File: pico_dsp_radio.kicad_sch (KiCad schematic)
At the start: 12 parts, among them J1 Conn_01x02, Q1 IRLML6402, SW1 SW_SPDT, U1 Pico, U2 MCP73831-2-OT

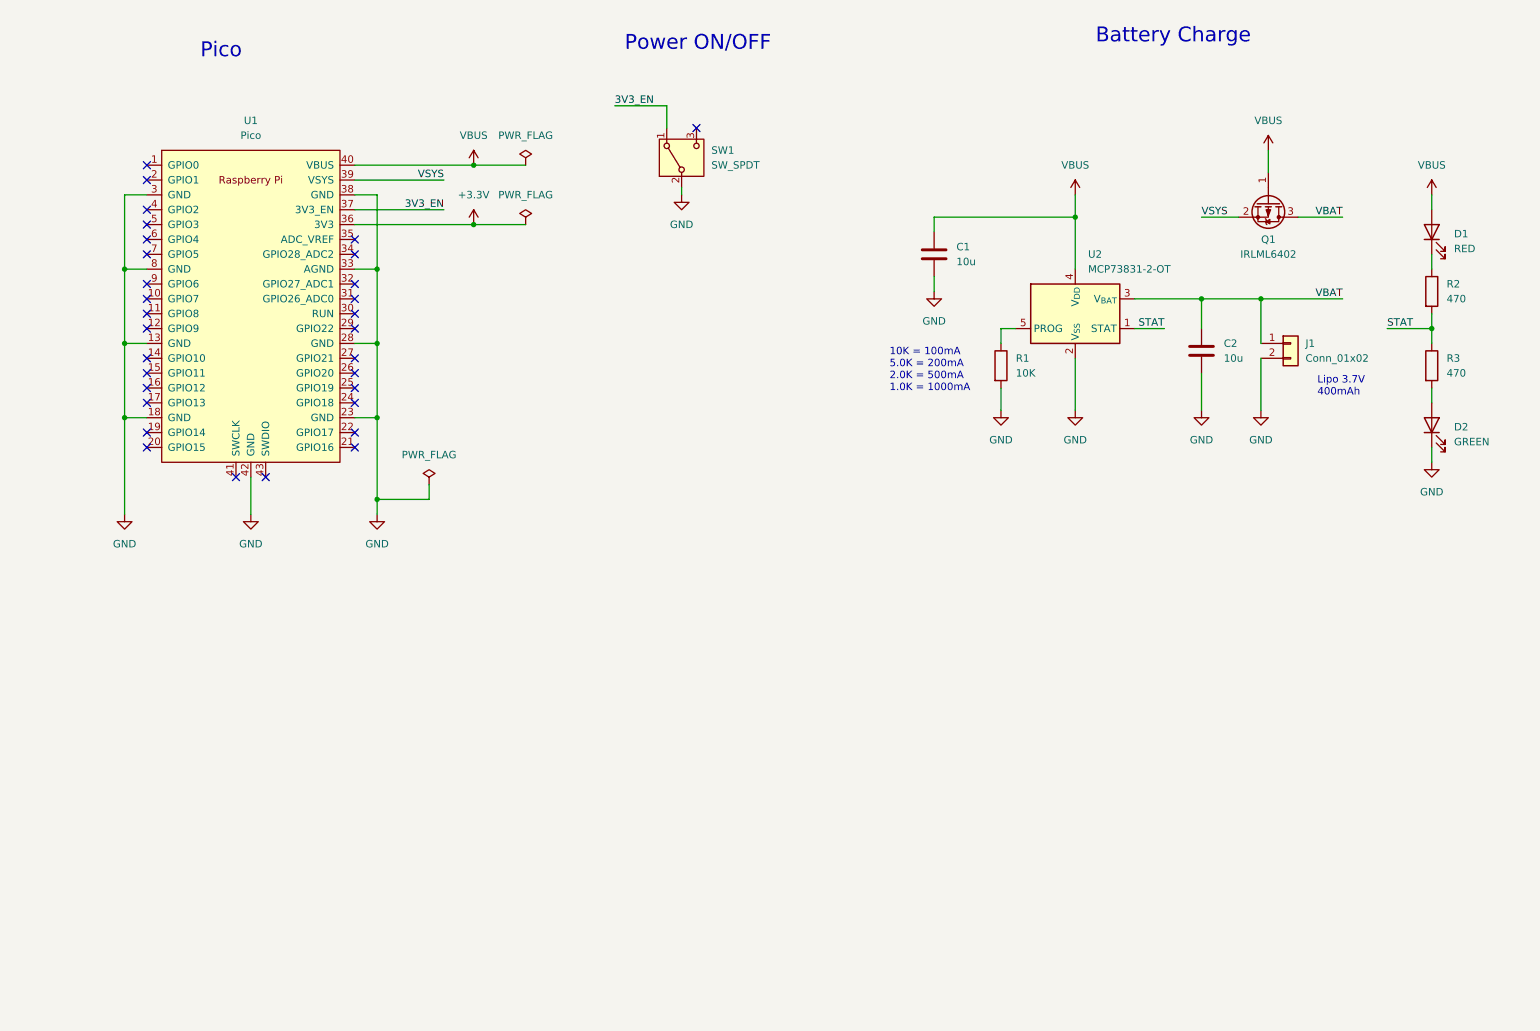
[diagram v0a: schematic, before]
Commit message: feat: Add Radio module
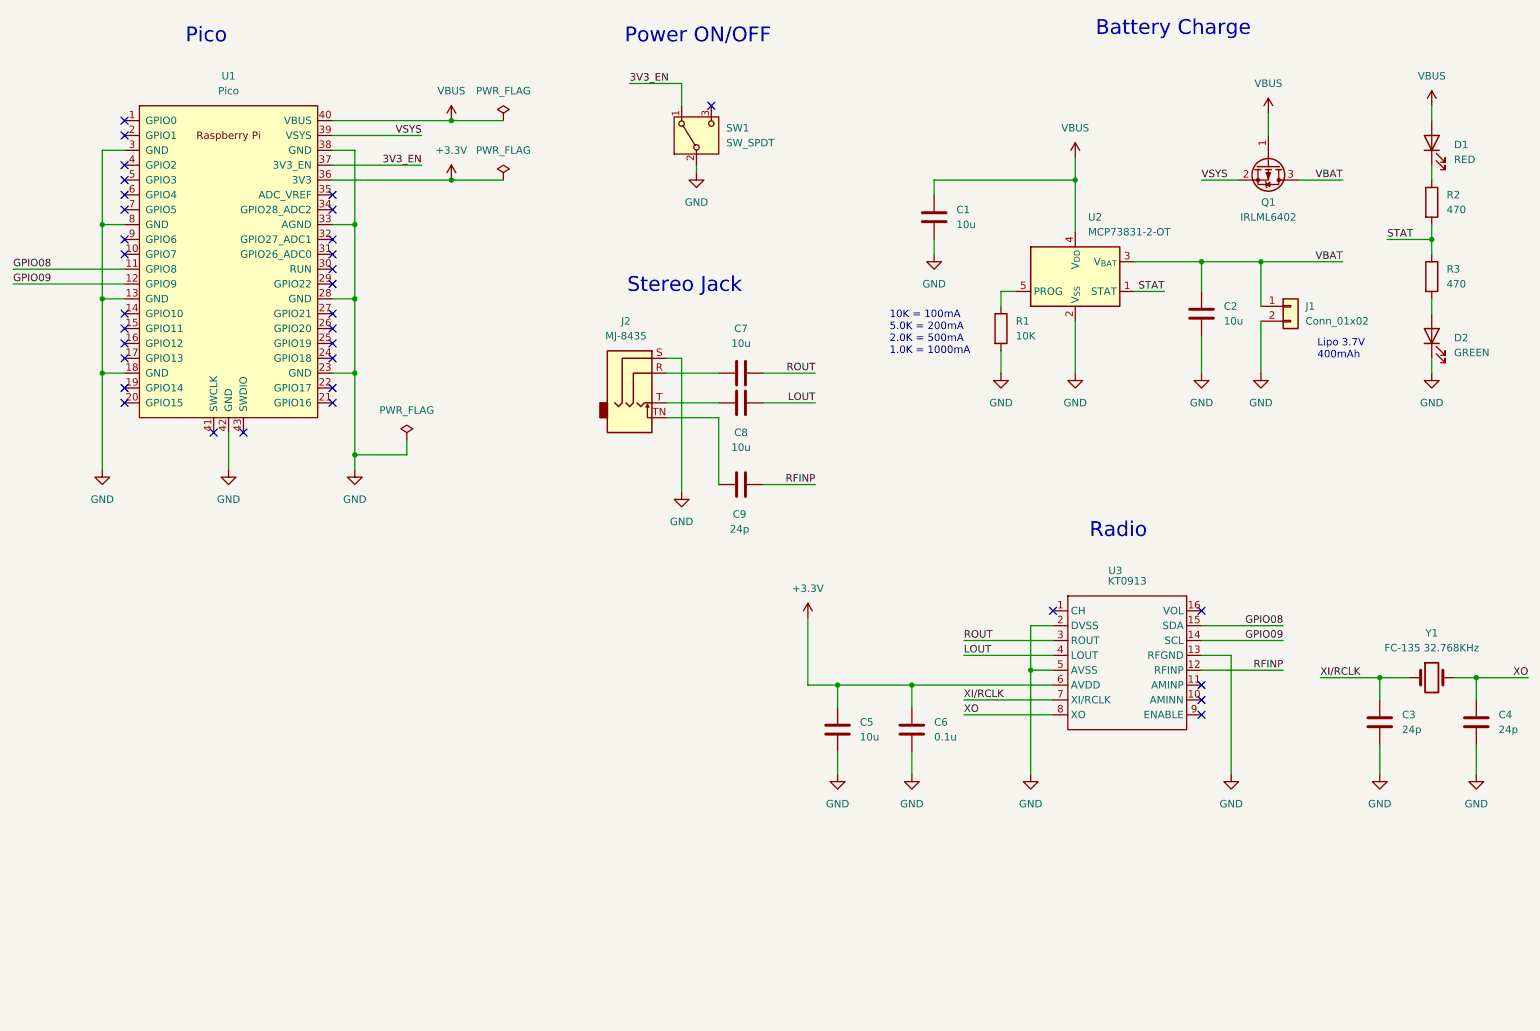
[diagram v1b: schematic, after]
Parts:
- added C3, C4, C9: 24p, symbol Device:C
- added C5, C7, C8: 10u, symbol Device:C
- added C6: 0.1u, symbol Device:C
- added J2: MJ-8435, symbol Connector_Audio:AudioJack3_SwitchT
- added U3: KT0913, Package_SO:SSOP-16_3.9x4.9mm_P0.635mm, symbol KTMicro:KT0913
- added Y1: FC-135 32.768KHz, symbol Device:Crystal
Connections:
- net +3.3V: now also C5.1, C6.1, U3.6 (AVDD)
- net GND: now also C3.2, C4.2, C5.2, C6.2, J2.S, U3.13 (RFGND), U3.2 (DVSS), U3.5 (AVSS)
- net GPIO08: now reaches U1.11 (GPIO8)
- net GPIO08: now also U3.15 (SDA)
- net GPIO09: now reaches U1.12 (GPIO9)
- net GPIO09: now also U3.14 (SCL)
- new net: C7.1, J2.R
- new net: C9.1, J2.TN
- new net: C8.2, J2.T
- new net LOUT: C8.1, U3.4 (LOUT)
- new net RFINP: C9.2, U3.12 (RFINP)
- new net ROUT: C7.2, U3.3 (ROUT)
- new net XI/RCLK: C3.1, U3.7 (XI/RCLK), Y1.1
- new net XO: C4.1, U3.8 (XO), Y1.2
- no-connect marks 31 -> 34
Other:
- note added: "Radio"
- note added: "Stereo Jack"
- moved on the sheet: C1, C2, D1, D2, J1, Q1, R1, R2, R3, SW1, U1, U2

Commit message: feat: Add TFT LCD
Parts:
- added J3: Conn_01x12, symbol Connector_Generic:Conn_01x12
- added R4: 10, symbol Device:R
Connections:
- net +3.3V: now also J3.4 (Pin_4), R4.1
- net GND: now also J3.1 (Pin_1), J3.12 (Pin_12), J3.2 (Pin_2), J3.5 (Pin_5), J3.6 (Pin_6)
- net GPIO08: now also J3.7 (Pin_7); no longer U3.15 (SDA)
- net GPIO09: now also J3.8 (Pin_8); no longer U3.14 (SCL)
- net GPIO10: now reaches U1.14 (GPIO10)
- net GPIO10: now also J3.9 (Pin_9)
- net GPIO11: now reaches U1.15 (GPIO11)
- net GPIO11: now also J3.10 (Pin_10)
- net GPIO12: now reaches U1.16 (GPIO12)
- net GPIO12: now also J3.11 (Pin_11)
- net GPIO20: now reaches U1.26 (GPIO20)
- net GPIO20: now also U3.15 (SDA)
- net GPIO21: now reaches U1.27 (GPIO21)
- net GPIO21: now also U3.14 (SCL)
- new net: J3.3 (Pin_3), R4.2
- no-connect marks 34 -> 29
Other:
- note added: "ATM0130B3 SPI"
- note added: "KT0913 I2C"
- note added: "TFT LCD"
- note added: "TFT LCD ATM0130B3"

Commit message: feat: Add Channel and Volume adjustment
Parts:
- added RV1, RV2: RV100F-30-6K3B-B10K-B301, symbol Device:R_Potentiometer
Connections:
- net +3.3V: now also RV1.1, RV2.1
- net GND: now also RV1.3, RV2.3; no longer U1.42 (GND)
- net CH: now reaches U3.1 (CH)
- net CH: now also RV1.2
- net VOL: now reaches U3.16 (VOL)
- net VOL: now also RV2.2
- no-connect marks 29 -> 28
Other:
- note added: "Channel Adjustment"
- note added: "Volume Adjustment"

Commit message: feat: Changed the crystal oscillator model to a larger size
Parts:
- Y1: value FC-135 32.768KHz -> 32.768K12.5PI/4115E
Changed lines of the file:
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@@
 			)
 		)
-		(property "Value" "FC-135 32.768KHz"
+		(property "Value" "32.768K12.5PI/4115E"
 			(at 261.62 130.81 0)
 			(effects
